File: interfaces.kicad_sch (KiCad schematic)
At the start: 36 parts, among them J4 1140084168, J5 0473460001, U1 TS3USB30EDGSR, U5 TS3USB30EDGSR, U6 FT234XD-R

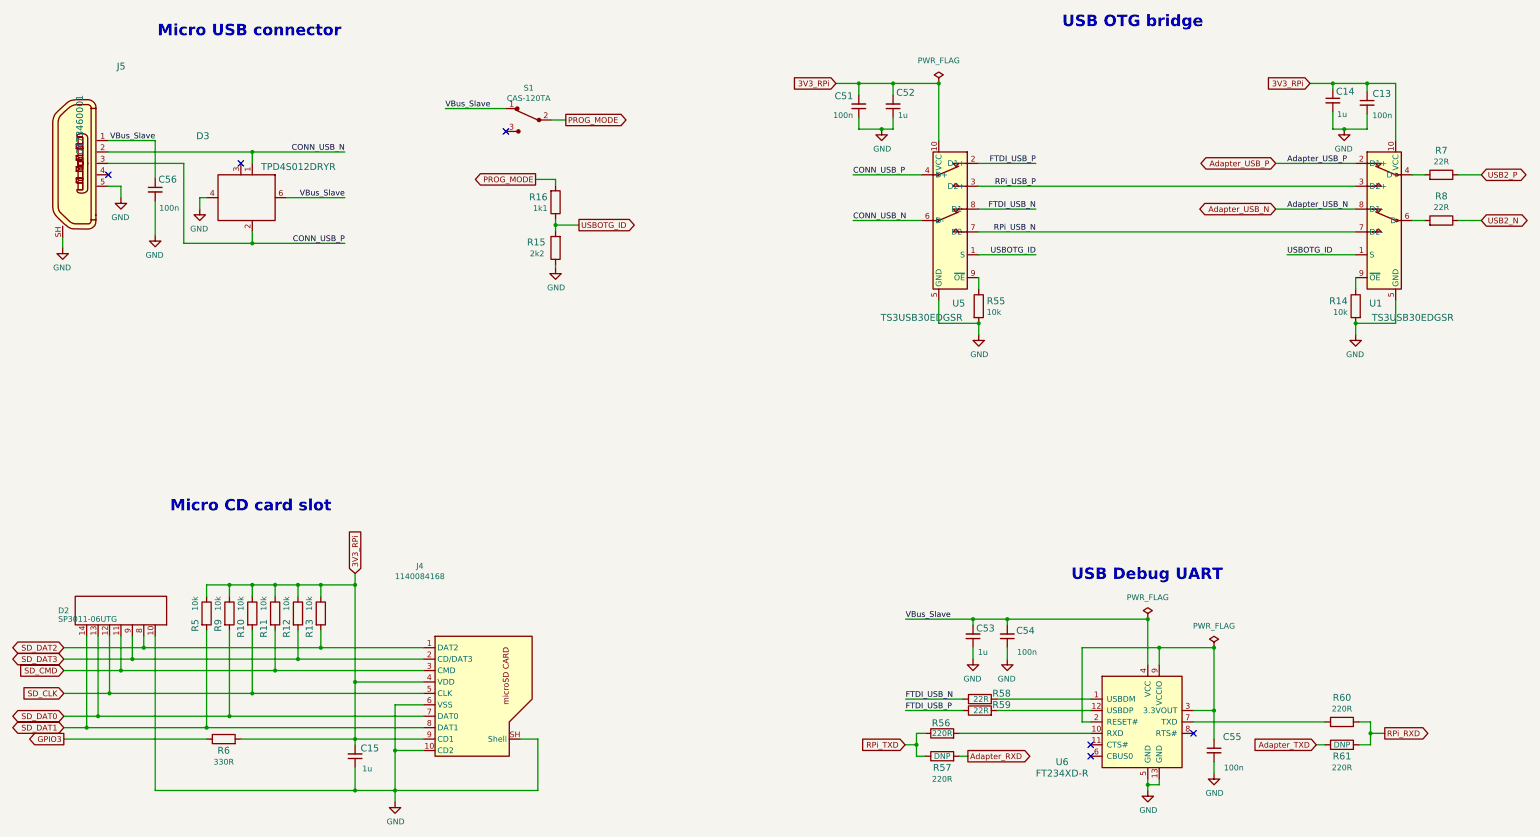
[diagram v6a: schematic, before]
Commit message: Update R5, R9, R10, R11, R12, R13, R14, R19, R55, R65 symbol and footprint
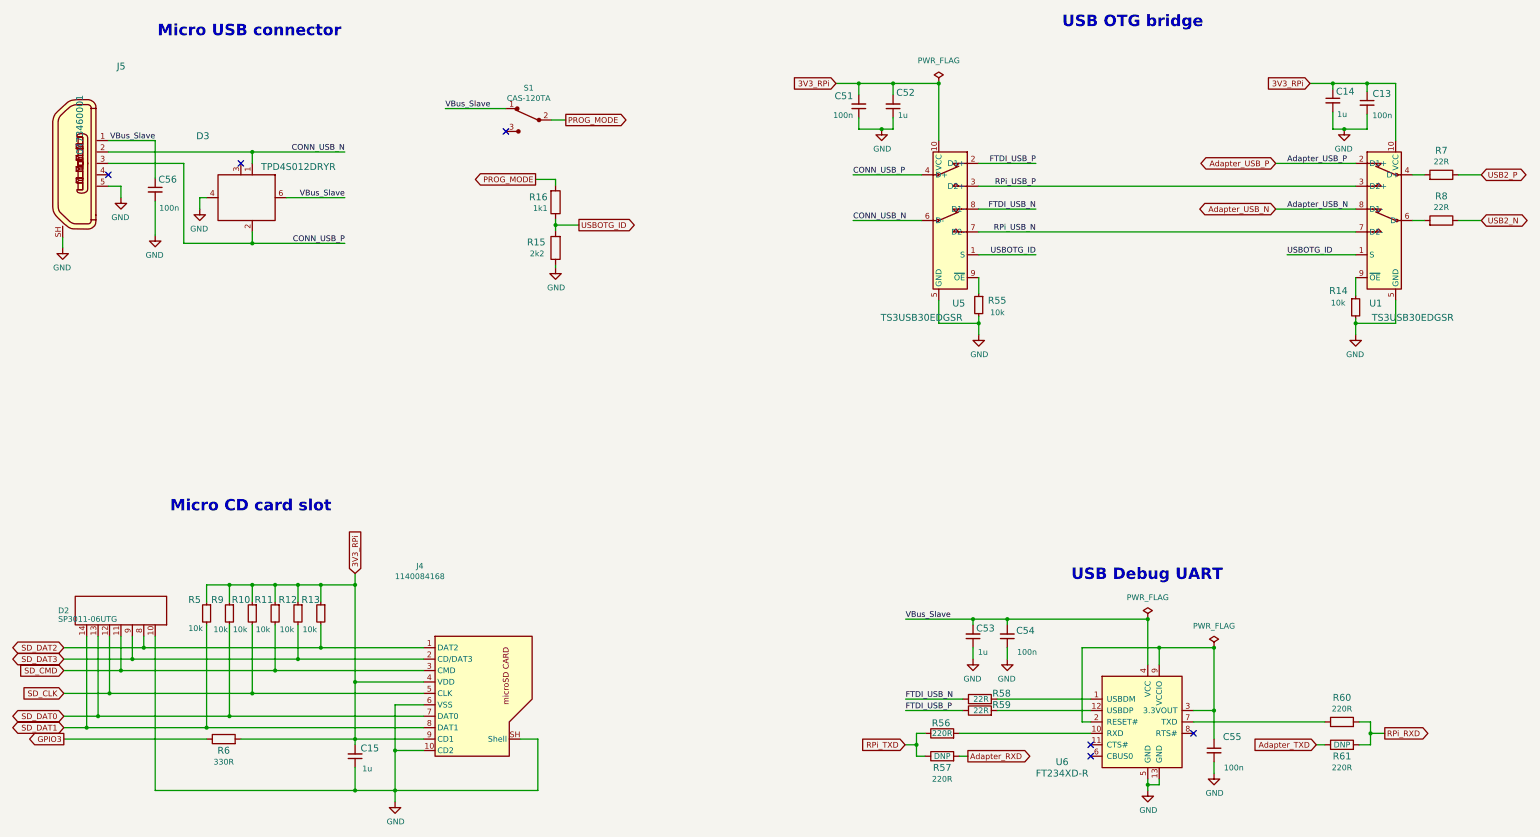
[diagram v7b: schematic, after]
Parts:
- R10, R11, R12, R13, R14, R5, R55, R9: footprint scalenode-cm4-baseboard-footprints:0402-res -> antmicro-footprints:R_0402_1005Metric; symbol scalenode-cm4-baseboard:R_10k_0402 -> antmicroResistors0402:R_10k_0402; Author (none) -> Antmicro; License (none) -> Apache-2.0; MPN CRCW040210K0FKEDHP -> CR0402-FX-1002GLF; Manufacturer VISHAY -> Bourns; Tolerance (none) -> 1%

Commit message: Update R7, R8, R58, R59 symbol and footprint
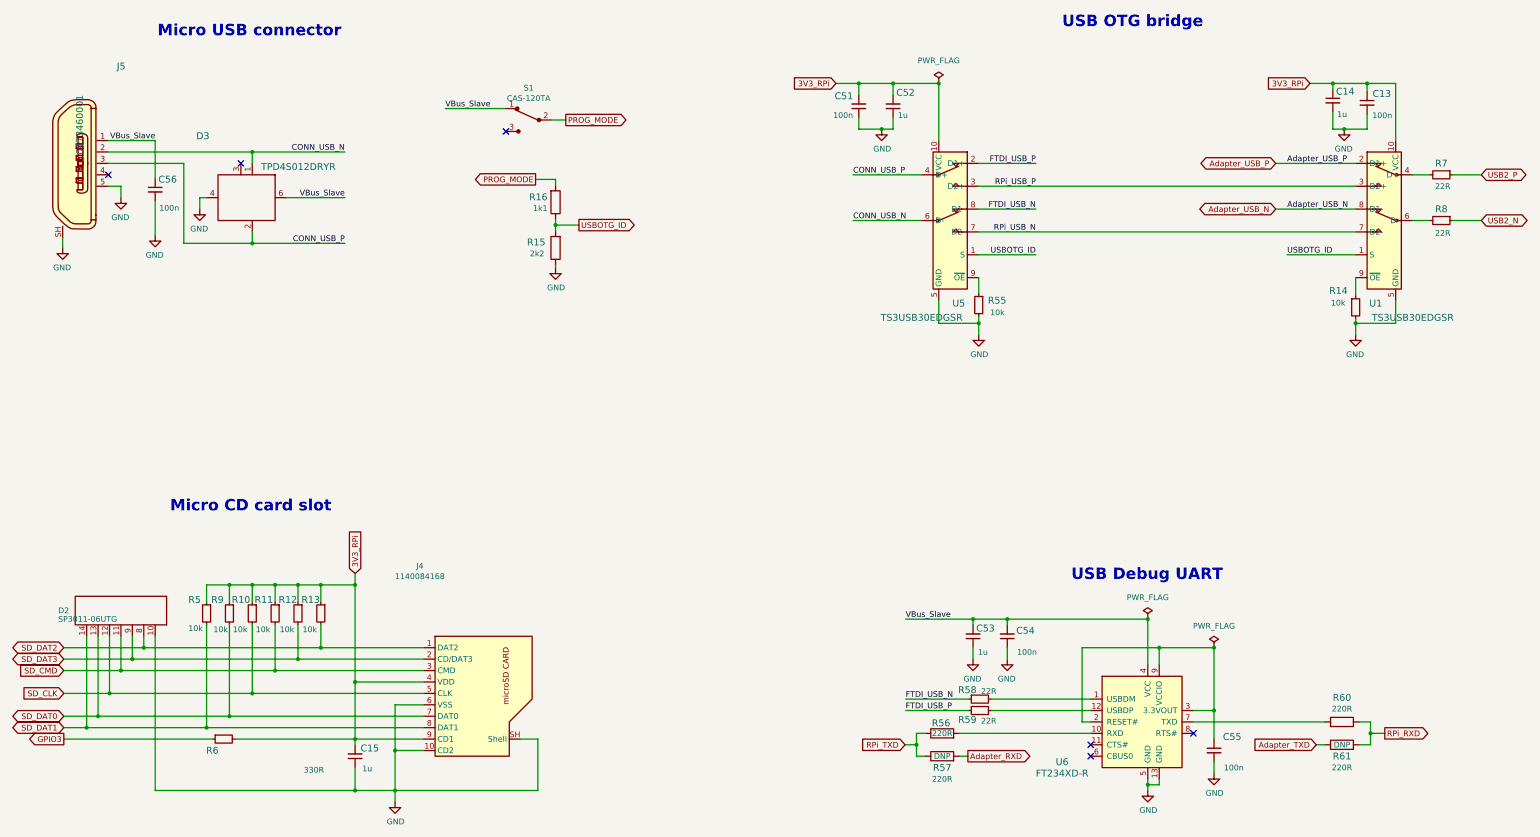
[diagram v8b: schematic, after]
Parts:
- R58, R59, R7, R8: footprint scalenode-cm4-baseboard-footprints:0402-res -> antmicro-footprints:R_0402_1005Metric; symbol scalenode-cm4-baseboard:R_22R_0402 -> antmicroResistors0402:R_22R_0402; Author (none) -> Antmicro; License (none) -> Apache-2.0; MPN CRCW040222R0FKED -> CR0402-FX-22R0GLF; Manufacturer VISHAY -> Bourns; Tolerance (none) -> 1%
- R6: footprint scalenode-cm4-baseboard-footprints:0402-res -> antmicro-footprints:R_0402_1005Metric; symbol scalenode-cm4-baseboard:R_330R_0402 -> antmicroResistors0402:R_330R_0402; Author (none) -> Antmicro; License (none) -> Apache-2.0; MPN MCMR04X3300FTL -> CR0402-FX-3300GLF; Manufacturer MULTICOMP -> Bourns; Tolerance (none) -> 1%
